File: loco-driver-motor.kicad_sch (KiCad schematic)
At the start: 20 parts, among them U801 BDR6133

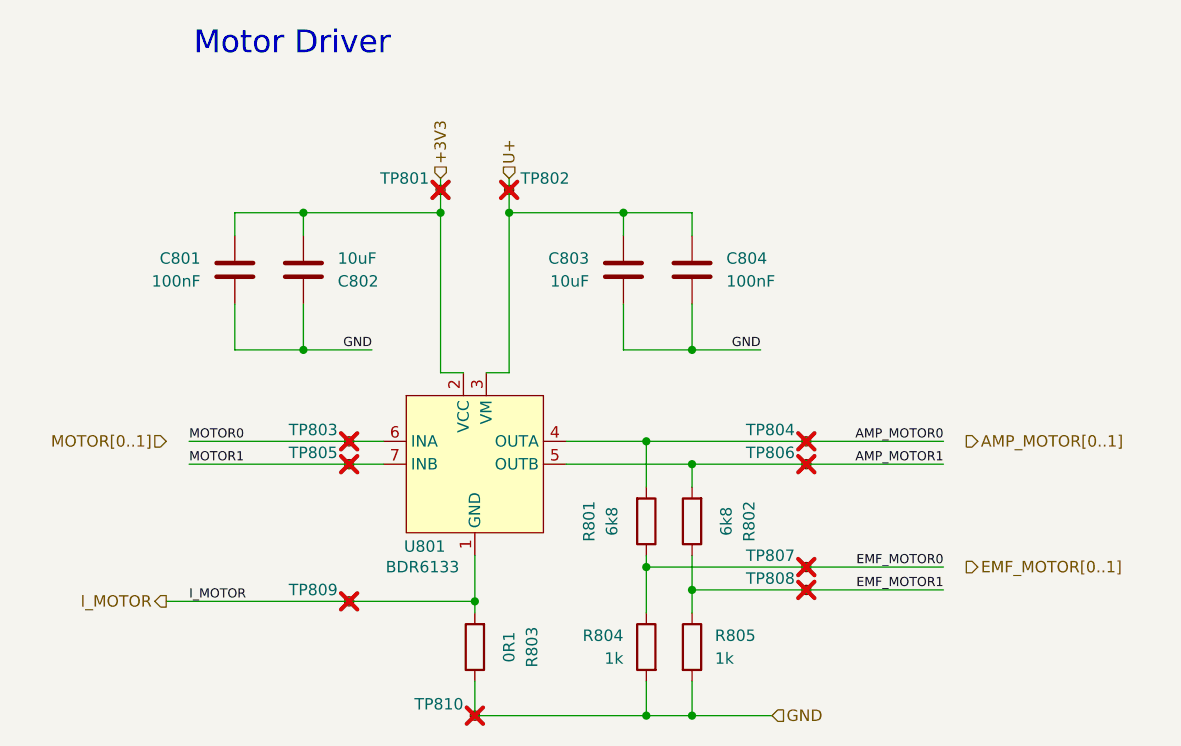
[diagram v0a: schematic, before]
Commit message: Fix - Remove ERC error, refresh annotation
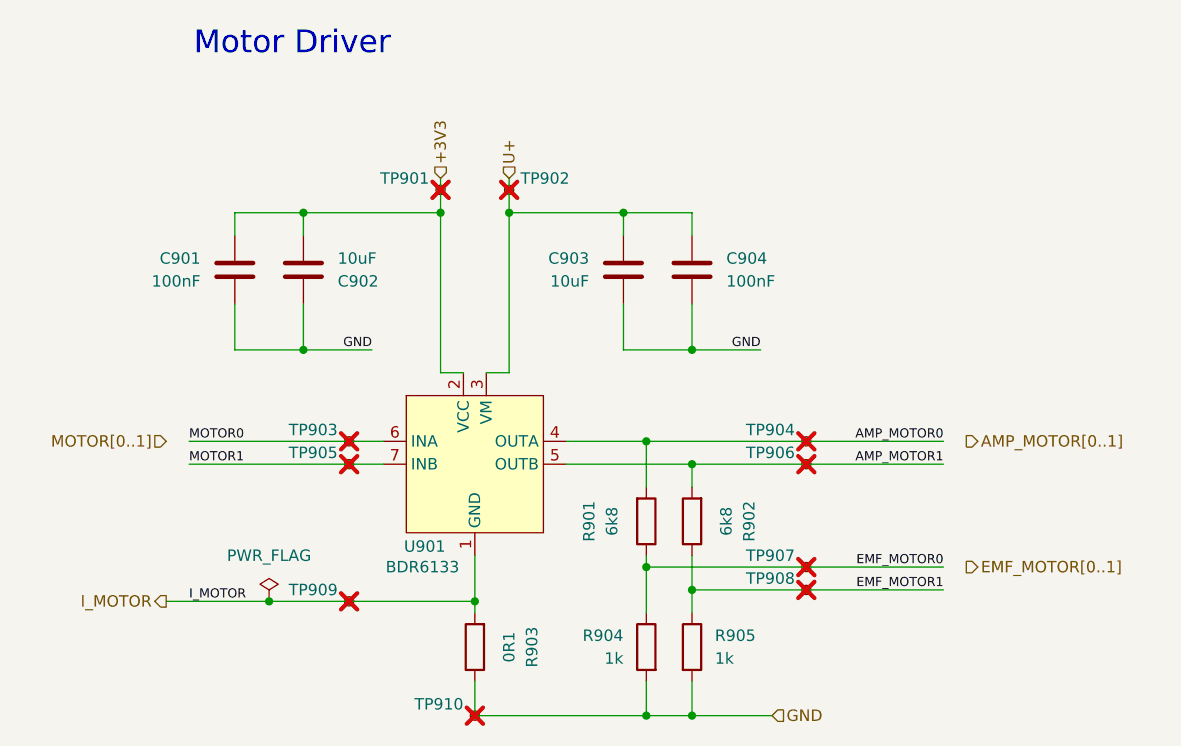
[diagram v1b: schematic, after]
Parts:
- renumbered C801 to C901, C802 to C902, C803 to C903, C804 to C904, R801 to R901, R802 to R902, R803 to R903, R804 to R904, R805 to R905, TP801 to TP901, TP802 to TP902, TP803 to TP903, TP804 to TP904, TP805 to TP905, TP806 to TP906, TP807 to TP907, TP808 to TP908, TP809 to TP909, TP810 to TP910, U801 to U901
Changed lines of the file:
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@@
+	)
+	(junction
+		(at 43.18 91.44)
+		(diameter 0)
+		(color 0 0 0 0)
 	)
 	(junction
@@
 	(wire
 		(pts
+			(xy 43.18 91.44) (xy 52.07 91.44)
+		)
+		(stroke
+			(width 0)
+			(type default)
+		)
+	)
+	(wire
+		(pts
 			(xy 66.04 100.33) (xy 66.04 104.14)
 		)
@@
 	(wire
 		(pts
-			(xy 31.75 91.44) (xy 52.07 91.44)
+			(xy 31.75 91.44) (xy 43.18 91.44)
 		)
 		(stroke
@@
 		(on_board no)
 		(dnp yes)
-		(property "Reference" "TP806"
+		(property "Reference" "TP906"
 			(at 101.6 74.9299 0)
 			(effects
@@
 			(project "xDuinoRails-Thor-M"
 				(path "/fb33ec4e-6596-45d2-a121-8d3475acd69a/28e0fa6a-354f-41d6-8b58-d1dd784eb1fe"
-					(reference "TP806")
+					(reference "TP906")
 					(unit 1)
 				)
@@
 		(on_board yes)
 		(dnp no)
-		(property "Reference" "U801"
+		(property "Reference" "U901"
 			(at 58.166 85.344 0)
 			(effects
@@
 			(project "xDuinoRails-Thor-M"
 				(path "/fb33ec4e-6596-45d2-a121-8d3475acd69a/28e0fa6a-354f-41d6-8b58-d1dd784eb1fe"
-					(reference "U801")
+					(reference "U901")
 					(unit 1)
 				)
@@
 		(on_board yes)
 		(dnp no)
-		(property "Reference" "R803"
+		(property "Reference" "R903"
 			(at 72.39 96.52 90)
 			(effects
@@
 			(project "xDuinoRails-Thor-M"
 				(path "/fb33ec4e-6596-45d2-a121-8d3475acd69a/28e0fa6a-354f-41d6-8b58-d1dd784eb1fe"
-					(reference "R803")
+					(reference "R903")
 					(unit 1)
 				)
@@
 		(on_board yes)
 		(dnp no)
-		(property "Reference" "R802"
+		(property "Reference" "R902"
 			(at 96.52 82.55 90)
 			(effects
@@
 			(project "xDuinoRails-Thor-M"
 				(path "/fb33ec4e-6596-45d2-a121-8d3475acd69a/28e0fa6a-354f-41d6-8b58-d1dd784eb1fe"
-					(reference "R802")
+					(reference "R902")
+					(unit 1)
+				)
+			)
+		)
+	)
+	(symbol
+		(lib_id "power:PWR_FLAG")
+		(at 43.18 91.44 0)
+		(unit 1)
+		(exclude_from_sim no)
+		(in_bom yes)
+		(on_board yes)
+		(dnp no)
+		(fields_autoplaced yes)
+		(property "Reference" "#FLG901"
+			(at 43.18 89.535 0)
+			(effects
+				(font
+					(size 1.27 1.27)
+				)
+				(hide yes)
+			)
+		)
+		(property "Value" "PWR_FLAG"
+			(at 43.18 86.36 0)
+			(effects
+				(font
+					(size 1.27 1.27)
+				)
+			)
+		)
+		(property "Footprint" ""
+			(at 43.18 91.44 0)
+			(effects
+				(font
+					(size 1.27 1.27)
+				)
+				(hide yes)
+			)
+		)
+		(property "Datasheet" "~"
+			(at 43.18 91.44 0)
+			(effects
+				(font
+					(size 1.27 1.27)
+				)
+				(hide yes)
+			)
+		)
+		(property "Description" "Special symbol for telling ERC where power comes from"
+			(at 43.18 91.44 0)
+			(effects
+				(font
+					(size 1.27 1.27)
+				)
+				(hide yes)
+			)
+		)
+		(pin "1"
+		)
+		(instances
+			(project ""
+				(path "/fb33ec4e-6596-45d2-a121-8d3475acd69a/28e0fa6a-354f-41d6-8b58-d1dd784eb1fe"
+					(reference "#FLG901")
 					(unit 1)
 				)
@@
 		(on_board no)
 		(dnp yes)
-		(property "Reference" "TP809"
+		(property "Reference" "TP909"
 			(at 50.8 90.1699 0)
 			(effects
@@
 			(project "xDuinoRails-Thor-M"
 				(path "/fb33ec4e-6596-45d2-a121-8d3475acd69a/28e0fa6a-354f-41d6-8b58-d1dd784eb1fe"
-					(reference "TP809")
+					(reference "TP909")
 					(unit 1)
 				)
@@
 		(dnp no)
 		(fields_autoplaced yes)
-		(property "Reference" "R801"
+		(property "Reference" "R901"
 			(at 78.74 82.55 90)
 			(effects
@@
 			(project "xDuinoRails-Thor-M"
 				(path "/fb33ec4e-6596-45d2-a121-8d3475acd69a/28e0fa6a-354f-41d6-8b58-d1dd784eb1fe"
-					(reference "R801")
+					(reference "R901")
 					(unit 1)
 				)
@@
 		(on_board no)
 		(dnp yes)
-		(property "Reference" "TP804"
+		(property "Reference" "TP904"
 			(at 101.6 72.3899 0)
 			(effects
@@
 			(project "xDuinoRails-Thor-M"
 				(path "/fb33ec4e-6596-45d2-a121-8d3475acd69a/28e0fa6a-354f-41d6-8b58-d1dd784eb1fe"
-					(reference "TP804")
+					(reference "TP904")
 					(unit 1)
 				)
@@
 		(on_board no)
 		(dnp yes)
-		(property "Reference" "TP808"
+		(property "Reference" "TP908"
 			(at 101.6 88.8999 0)
 			(effects
@@
 			(project "xDuinoRails-Thor-M"
 				(path "/fb33ec4e-6596-45d2-a121-8d3475acd69a/28e0fa6a-354f-41d6-8b58-d1dd784eb1fe"
-					(reference "TP808")
+					(reference "TP908")
 					(unit 1)
 				)
@@
 		(on_board no)
 		(dnp yes)
-		(property "Reference" "TP802"
+		(property "Reference" "TP902"
 			(at 71.12 44.4499 0)
 			(effects
@@
 			(project "xDuinoRails-Thor-M"
 				(path "/fb33ec4e-6596-45d2-a121-8d3475acd69a/28e0fa6a-354f-41d6-8b58-d1dd784eb1fe"
-					(reference "TP802")
+					(reference "TP902")
 					(unit 1)
 				)
@@
 		(dnp no)
 		(fields_autoplaced yes)
-		(property "Reference" "C804"
+		(property "Reference" "C904"
 			(at 93.98 53.3399 0)
 			(effects
@@
 			(project "xDuinoRails-Thor-M"
 				(path "/fb33ec4e-6596-45d2-a121-8d3475acd69a/28e0fa6a-354f-41d6-8b58-d1dd784eb1fe"
-					(reference "C804")
+					(reference "C904")
 					(unit 1)
 				)
@@
 		(on_board no)
 		(dnp yes)
-		(property "Reference" "TP801"
+		(property "Reference" "TP901"
 			(at 60.96 44.4499 0)
 			(effects
@@
 			(project "xDuinoRails-Thor-M"
 				(path "/fb33ec4e-6596-45d2-a121-8d3475acd69a/28e0fa6a-354f-41d6-8b58-d1dd784eb1fe"
-					(reference "TP801")
+					(reference "TP901")
 					(unit 1)
 				)
@@
 		(dnp no)
 		(fields_autoplaced yes)
-		(property "Reference" "R804"
+		(property "Reference" "R904"
 			(at 82.55 95.2499 0)
 			(effects
@@
 			(project "xDuinoRails-Thor-M"
 				(path "/fb33ec4e-6596-45d2-a121-8d3475acd69a/28e0fa6a-354f-41d6-8b58-d1dd784eb1fe"
-					(reference "R804")
+					(reference "R904")
 					(unit 1)
 				)
@@
 		(on_board no)
 		(dnp yes)
-		(property "Reference" "TP803"
+		(property "Reference" "TP903"
 			(at 50.8 72.3899 0)
 			(effects
@@
 			(project "xDuinoRails-Thor-M"
 				(path "/fb33ec4e-6596-45d2-a121-8d3475acd69a/28e0fa6a-354f-41d6-8b58-d1dd784eb1fe"
-					(reference "TP803")
+					(reference "TP903")
 					(unit 1)
 				)
@@
 		(on_board yes)
 		(dnp no)
-		(property "Reference" "C803"
+		(property "Reference" "C903"
 			(at 78.74 53.3399 0)
 			(effects
@@
 			(project "xDuinoRails-Thor-M"
 				(path "/fb33ec4e-6596-45d2-a121-8d3475acd69a/28e0fa6a-354f-41d6-8b58-d1dd784eb1fe"
-					(reference "C803")
+					(reference "C903")
 					(unit 1)
 				)
@@
 		(on_board no)
 		(dnp yes)
-		(property "Reference" "TP807"
+		(property "Reference" "TP907"
 			(at 101.6 86.3599 0)
 			(effects
@@
 			(project "xDuinoRails-Thor-M"
 				(path "/fb33ec4e-6596-45d2-a121-8d3475acd69a/28e0fa6a-354f-41d6-8b58-d1dd784eb1fe"
-					(reference "TP807")
+					(reference "TP907")
 					(unit 1)
 				)
@@
 		(on_board no)
 		(dnp yes)
-		(property "Reference" "TP810"
+		(property "Reference" "TP910"
 			(at 64.77 102.8699 0)
 			(effects
@@
 			(project "xDuinoRails-Thor-M"
 				(path "/fb33ec4e-6596-45d2-a121-8d3475acd69a/28e0fa6a-354f-41d6-8b58-d1dd784eb1fe"
-					(reference "TP810")
+					(reference "TP910")
 					(unit 1)
 				)
@@
 		(dnp no)
 		(fields_autoplaced yes)
-		(property "Reference" "C801"
+		(property "Reference" "C901"
 			(at 35.56 53.3399 0)
 			(effects
@@
 			(project "xDuinoRails-Thor-M"
 				(path "/fb33ec4e-6596-45d2-a121-8d3475acd69a/28e0fa6a-354f-41d6-8b58-d1dd784eb1fe"
-					(reference "C801")
+					(reference "C901")
 					(unit 1)
 				)
@@
 		(on_board yes)
 		(dnp no)
-		(property "Reference" "C802"
+		(property "Reference" "C902"
 			(at 50.8 55.8801 0)
 			(effects
@@
 			(project "xDuinoRails-Thor-M"
 				(path "/fb33ec4e-6596-45d2-a121-8d3475acd69a/28e0fa6a-354f-41d6-8b58-d1dd784eb1fe"
-					(reference "C802")
+					(reference "C902")
 					(unit 1)
 				)
@@
 		(on_board no)
 		(dnp yes)
-		(property "Reference" "TP805"
+		(property "Reference" "TP905"
 			(at 50.8 74.9299 0)
 			(effects
@@
 			(project "xDuinoRails-Thor-M"
 				(path "/fb33ec4e-6596-45d2-a121-8d3475acd69a/28e0fa6a-354f-41d6-8b58-d1dd784eb1fe"
-					(reference "TP805")
+					(reference "TP905")
 					(unit 1)
 				)
@@
 		(on_board yes)
 		(dnp no)
-		(property "Reference" "R805"
+		(property "Reference" "R905"
 			(at 92.71 95.2499 0)
 			(effects
@@
 			(project "xDuinoRails-Thor-M"
 				(path "/fb33ec4e-6596-45d2-a121-8d3475acd69a/28e0fa6a-354f-41d6-8b58-d1dd784eb1fe"
-					(reference "R805")
+					(reference "R905")
 					(unit 1)
 				)
